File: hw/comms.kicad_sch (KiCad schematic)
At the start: 13 parts, among them J7 CAN IN, J8 CAN OUT, J9 USB-C, SW1 TERM, U6 TCAN3413, U7 USBLC6-2SC6

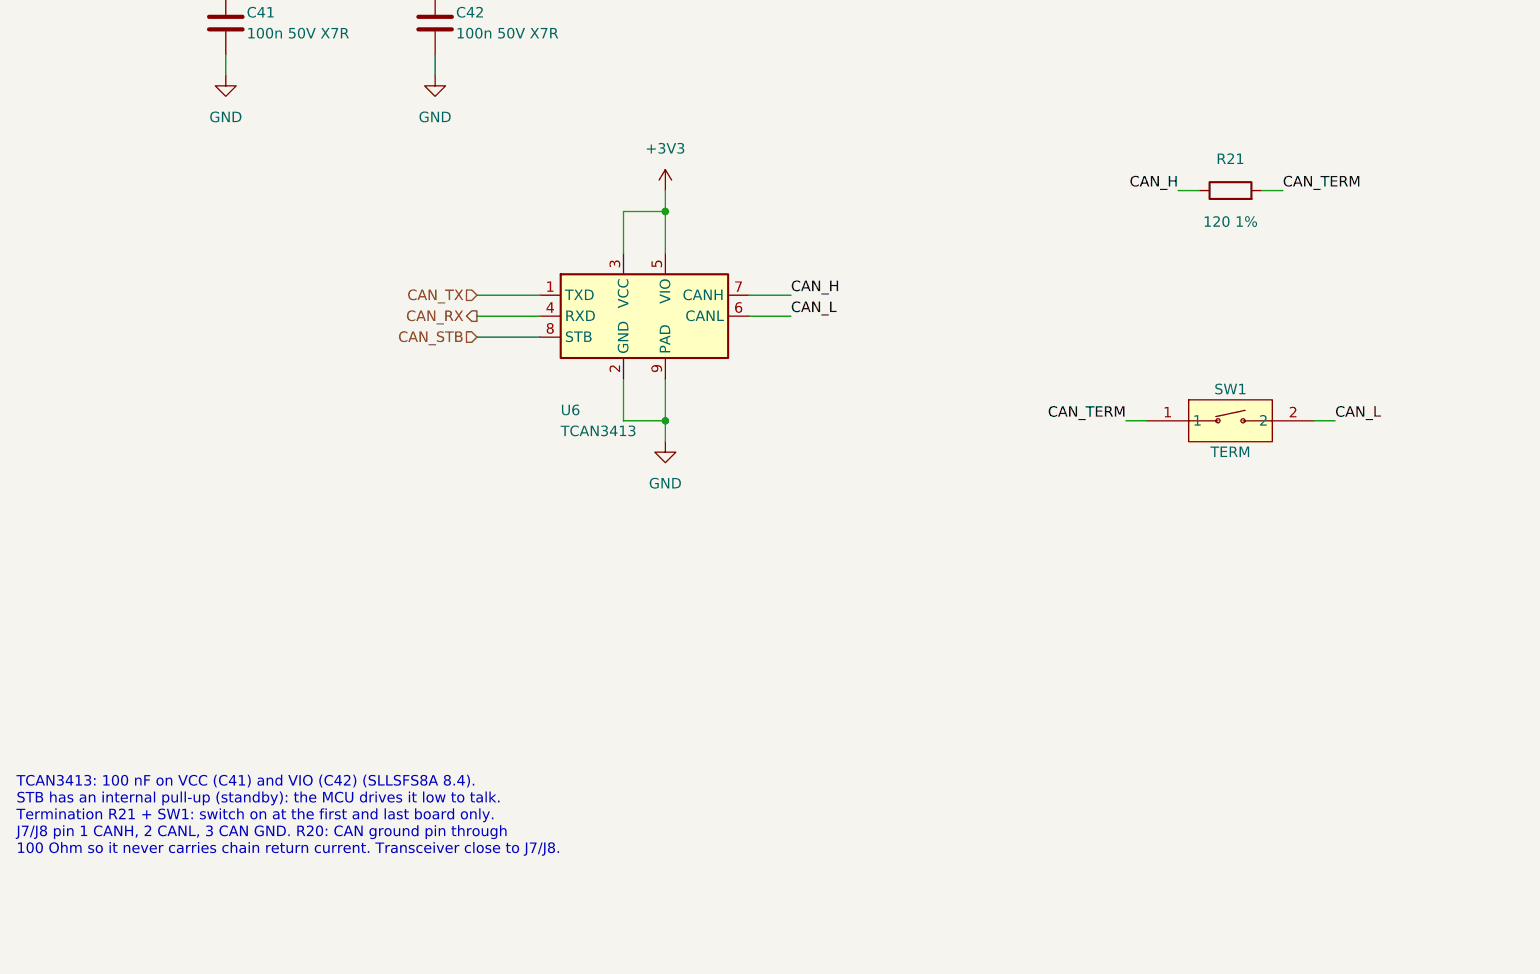
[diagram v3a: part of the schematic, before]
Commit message: Route the 6-layer board and finalize parts for ordering
The 45 x 45 mm board is fully routed on six layers (F / GND / SIG /
SIG / PWR / B, 2 oz outer, 1 oz inner): DRC 0 errors, 0 unconnected,
schematic parity 0. Four layers could not route the DRV-to-MCU links
without moving the power or input stage.

- Encoder shares the DRV8353's SPI3 bus, as on the PoC; PA5-PA7 are
  unused. R25 pulls DRV nSCS up, since the DRV's logic inputs have an
  internal pull-down. The SDO / MISO pin-type warning is an ERC
  exclusion with a note.
- MCU is now the STM32G473CEU6: the G474 without the unused HRTIM,
  checked pin for pin against both datasheets, in stock and cheaper.
- Male XT30PW-M power connectors, HCS1206 shunts, SWD pads at the
  board edge.
- Design doc and review notes updated for the new stack-up, shared
  bus and MCU.

Co-Authored-By: Claude Opus 5.5 <noreply@anthropic.com>
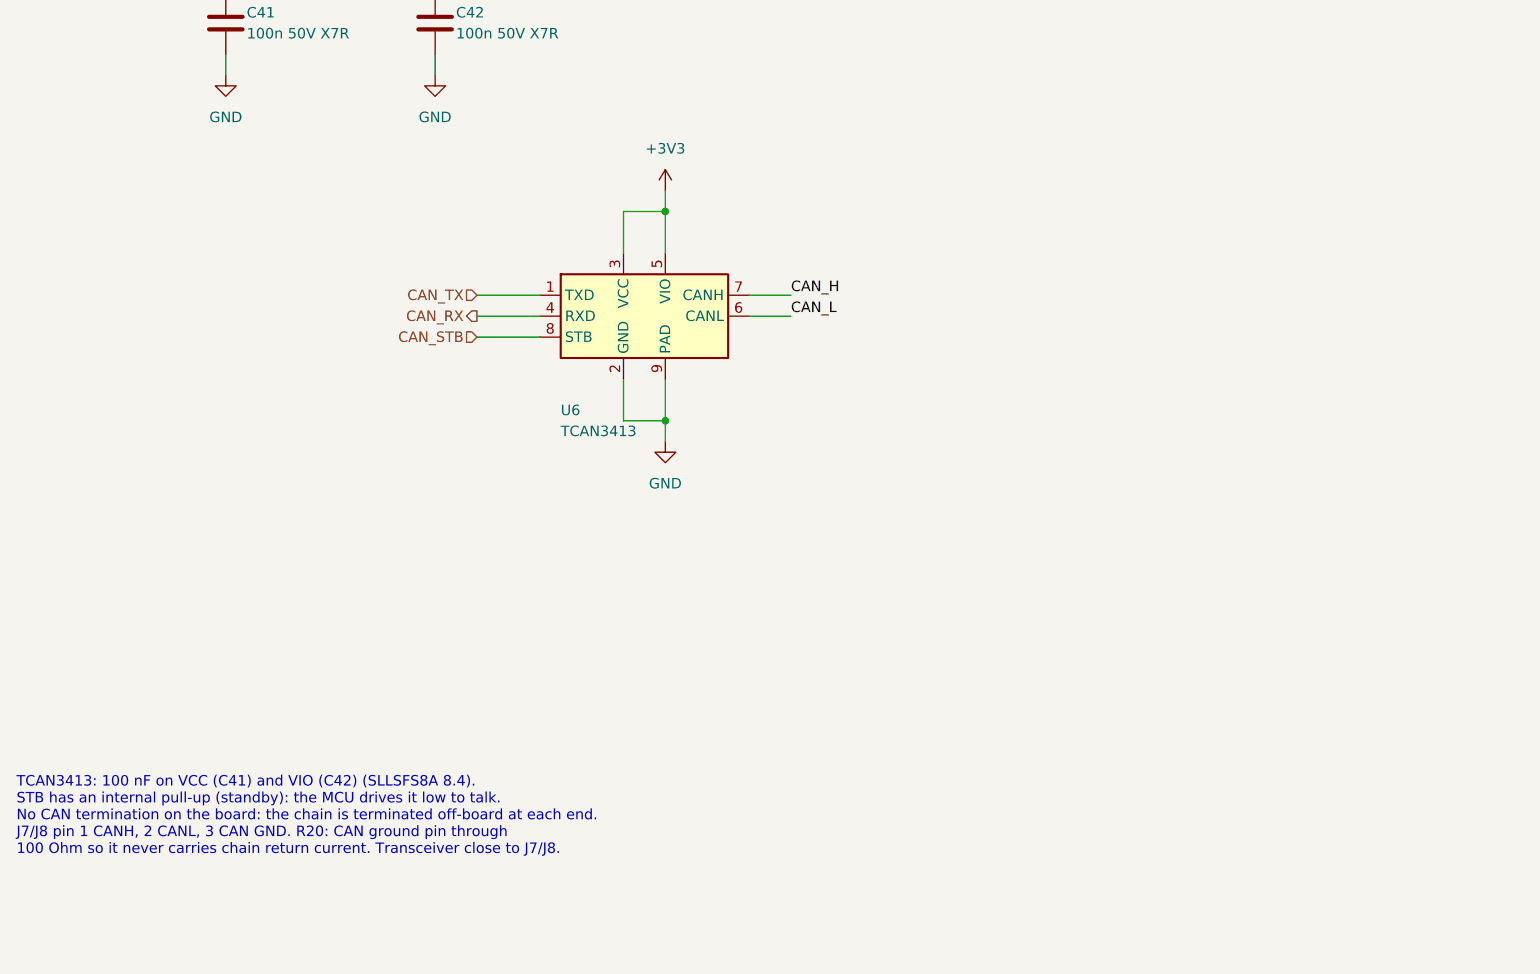
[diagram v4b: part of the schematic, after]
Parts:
- removed R21: 120 1%, Resistor_SMD:R_0603_1608Metric, symbol Device:R
- removed SW1: TERM, foc_controller:SW-SMD_1.27-1P-TPPT, symbol foc_controller:1.27-1PTPPT
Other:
- note added: "TCAN3413: 100 nF on VCC (C41) and VIO (C42) (SLLSFS8A 8.4). STB has an internal pull-up (standby): the MCU drives it low to talk. No CAN termination on the board: the chain is terminated off-board at each end. J7/J8 pin 1 CANH, 2 CANL, 3 CAN GND. R20: CAN ground pin through 100 Ohm so it never carries chain return current. Transceiver close to J7/J8."
- note removed: "TCAN3413: 100 nF on VCC (C41) and VIO (C42) (SLLSFS8A 8.4). STB has an internal pull-up (standby): the MCU drives it low to talk. Termination R21 + SW1: switch on at the first and last board only. J7/J8 pin 1 CANH, 2 CANL, 3 CAN GND. R20: CAN ground pin through 100 Ohm so it never carries chain return current. Transceiver close to J7/J8."
